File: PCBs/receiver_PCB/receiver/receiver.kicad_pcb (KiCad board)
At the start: 4 copper layers, 12 parts, among them U1 NRF54L15-CAAA-R

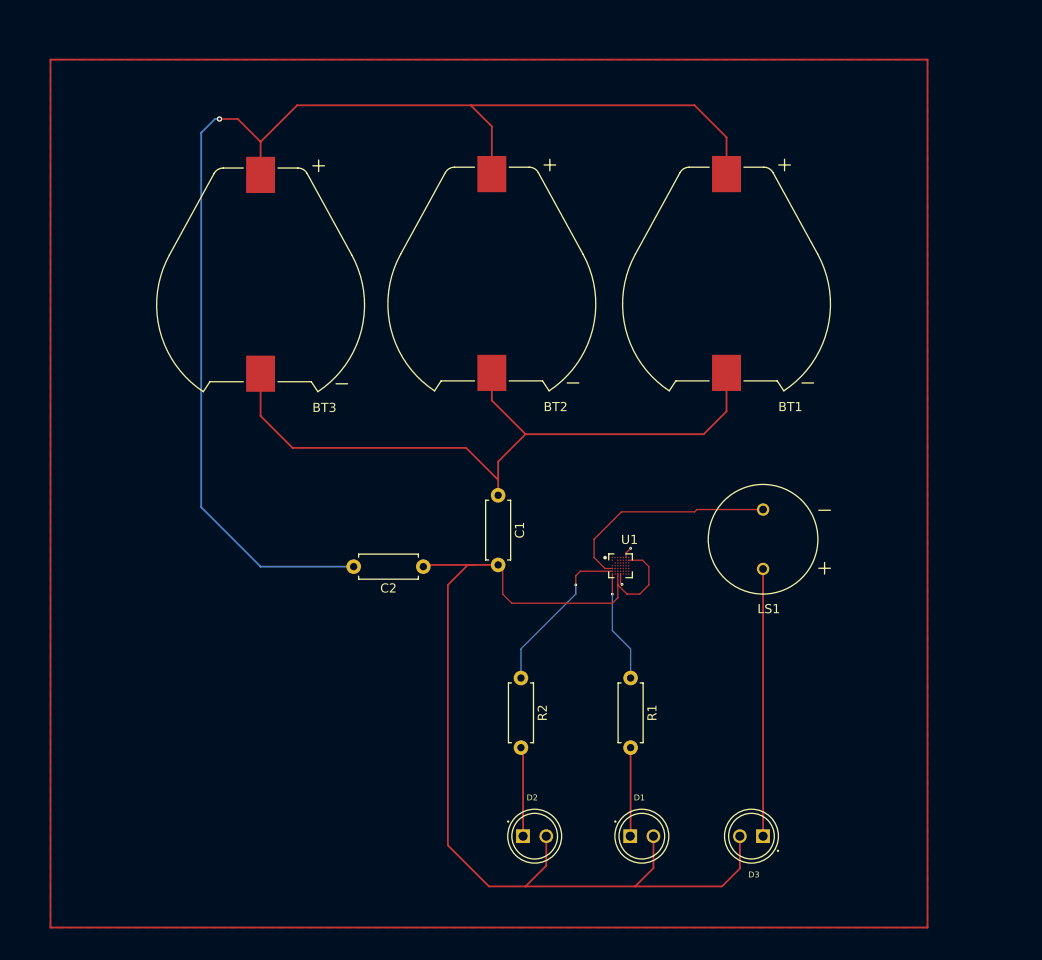
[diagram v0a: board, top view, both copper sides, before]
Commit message: add the 3rd pcb
Added new connector footprints, symbols, and STEP models for 2N2222, 2N2222A, BPW34, and 657002140201 in main_PCB_V1. Created new connector PCB project files. Updated .gitignore to exclude new backup and gerber directories. Modified early_energy_test_PCB to output gerbers to a dedicated folder and made minor PCB net and property adjustments.
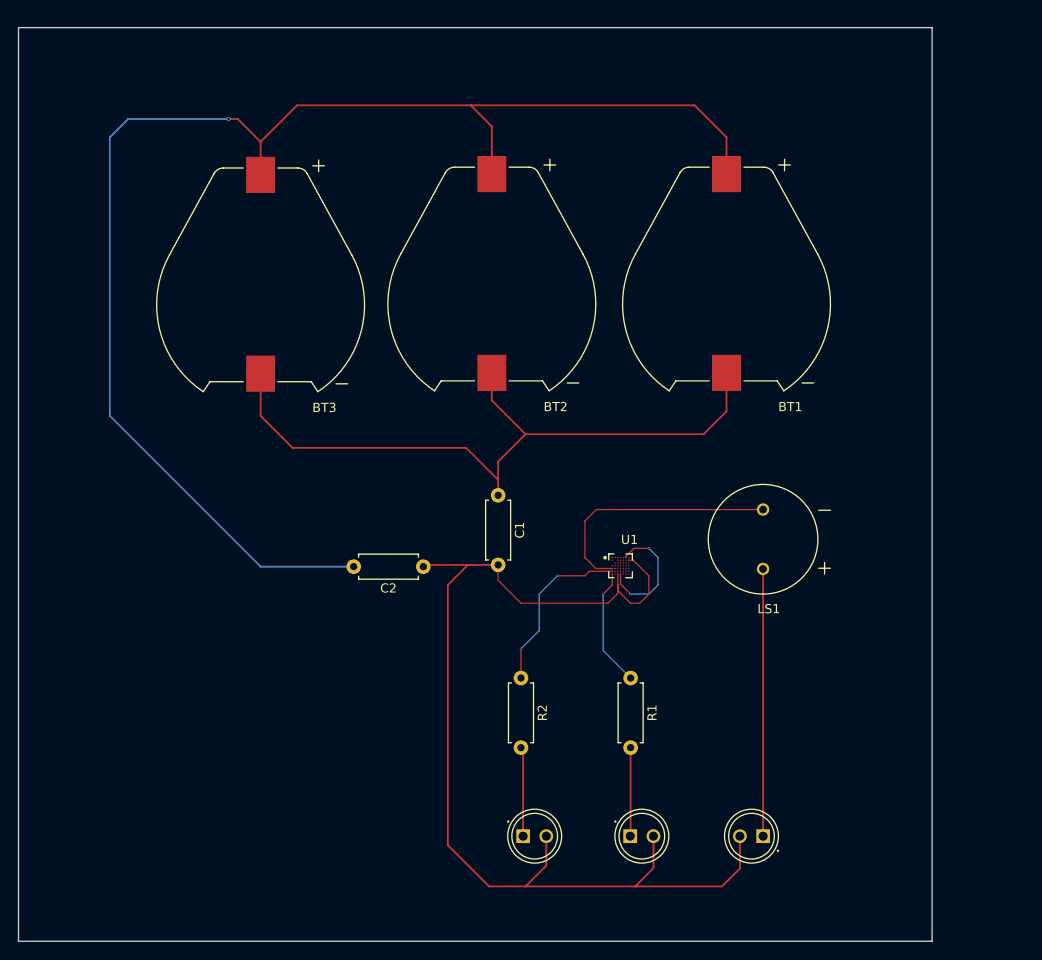
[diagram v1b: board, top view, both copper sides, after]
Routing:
- net GND: track 138.8 -> 152.6 mm
- net Net-(U1-P0.03): track 24.3 -> 27.5 mm
- net Net-(U1-P0.01): track 17.9 -> 19.1 mm, vias 1 -> 2
- net Net-(C1-Pad2): track 119.6 -> 120.7 mm
- net Net-(U1-VSS-PadA6): track 12.6 -> 13.5 mm
- net Net-(U1-P0.00): track 12.2 -> 13.0 mm
- removed copper zone on F.Cu, net (none)
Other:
- board outline added: 100 x 100 mm
- copper layers 4 -> 2

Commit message: Add soft_nRF_R project and update receiver PCB
Added new soft_nRF_R firmware project with initial source files. Updated receiver PCB design to use Wurth Elektronik connectors, revised net assignments, and replaced legacy footprints. Adjusted .gitignore for new build directory. Minor updates to other PCB and source files for consistency.
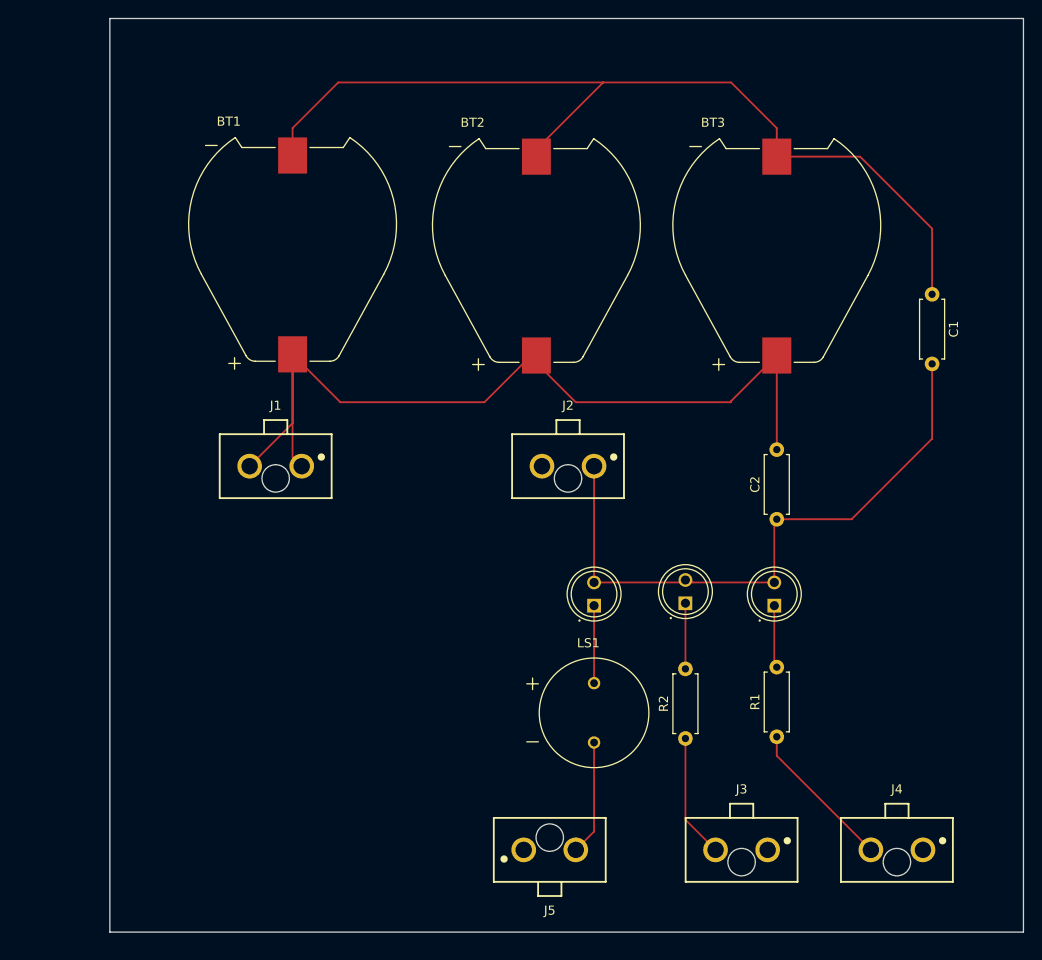
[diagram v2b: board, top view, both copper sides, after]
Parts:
- removed U1: NRF54L15-CAAA-R, PCB_footprints:BGA47N30P7X7_245X224X46N
- added J1: 6570XX140201_657002140201, PCB_footprints_connector:657002140201, F.Cu at (118.2, 100.0)
- added J2: 6570XX140201_657002140201, PCB_footprints_connector:657002140201, F.Cu at (150.2, 100.0)
- added J3: 6570XX140201_657002140201, PCB_footprints_connector:657002140201, F.Cu at (169.2, 142.0)
- added J4: 6570XX140201_657002140201, PCB_footprints_connector:657002140201, F.Cu at (186.2, 142.0)
- added J5: 6570XX140201_657002140201, PCB_footprints_connector:657002140201, F.Cu at (148.2, 142.0)
- moved BT3 56.5 mm to (173.0, 77.0), turned to 0 degrees
- moved C1 52.3 mm to (190.0, 81.2)
- moved BT1 47.5 mm to (120.0, 76.9), turned to 0 degrees
- moved C2 39.0 mm to (173.0, 105.8), turned to 90 degrees
- moved D3 31.6 mm to (153.0, 114.0), turned to 90 degrees
- moved D2 31.4 mm to (163.0, 113.7), turned to 90 degrees
- moved D1 30.2 mm to (172.7, 114.0), turned to 90 degrees
- moved LS1 26.5 mm to (153.0, 127.0), turned to 0 degrees
- moved R2 19.2 mm to (163.0, 129.8), turned to 90 degrees
- moved R1 17.2 mm to (173.0, 129.6), turned to 90 degrees
- moved BT2 5.24 mm to (146.7, 77.0), turned to 0 degrees
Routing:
- net GND: track 152.6 -> 99.2 mm, vias 1 -> 0
- net Net-(C1-Pad2): track 120.7 -> 68.6 mm
- net Net-(BT1-PadN): track 76.9 -> 101.9 mm
- net Net-(D3-PadC): track 29.2 -> 8.48 mm
- net Net-(J5-Pad2): track 27.5 -> 12.6 mm
- net Net-(U1-VSS-PadA6): track 13.5 -> 0.00 mm, vias 2 -> 0
- net Net-(J3-Pad2): track 19.1 -> 13.6 mm, vias 2 -> 0
- net Net-(J4-Pad2): track 13.0 -> 16.6 mm, vias 1 -> 0
- net Net-(D1-PadC): track 9.71 -> 6.84 mm
- net Net-(D2-PadC): track 9.79 -> 7.19 mm
